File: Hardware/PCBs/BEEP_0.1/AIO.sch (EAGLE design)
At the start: 86 parts, among them IC1 ULN2803ASOP18, IC2 ULN2803ASOP18, IC3 74HC238SSOP, IC4 74HC238SSOP, U2 TB6612FNG, U3 ATXMEGA64D3-AU, X10 MICROMATCH-10, X3 MICROMATCH-8, X4 MICROMATCH-8, X5 MICROMATCH-8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

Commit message: continue routing...
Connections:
- net IR_LED_MK0: now also U3.PF0; no longer U3.PF2
- net IR_LED_MK2: now also U3.PF2; no longer U3.PF0
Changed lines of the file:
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@@
 </segment>
 <segment>
-<wire x1="93.98" y1="86.36" x2="88.9" y2="86.36" width="0.1524" layer="91" style="longdash"/>
-<label x="88.9" y="86.36" size="1.27" layer="95" rot="R180" xref="yes"/>
-<pinref part="U3" gate="G$1" pin="PF2"/>
+<wire x1="93.98" y1="91.44" x2="88.9" y2="91.44" width="0.1524" layer="91" style="longdash"/>
+<label x="88.9" y="91.44" size="1.27" layer="95" rot="R180" xref="yes"/>
+<pinref part="U3" gate="G$1" pin="PF0"/>
 </segment>
 </net>
@@
 </segment>
 <segment>
-<wire x1="93.98" y1="91.44" x2="88.9" y2="91.44" width="0.1524" layer="91" style="longdash"/>
-<label x="88.9" y="91.44" size="1.27" layer="95" rot="R180" xref="yes"/>
-<pinref part="U3" gate="G$1" pin="PF0"/>
+<wire x1="93.98" y1="86.36" x2="88.9" y2="86.36" width="0.1524" layer="91" style="longdash"/>
+<label x="88.9" y="86.36" size="1.27" layer="95" rot="R180" xref="yes"/>
+<pinref part="U3" gate="G$1" pin="PF2"/>
 </segment>
 </net>

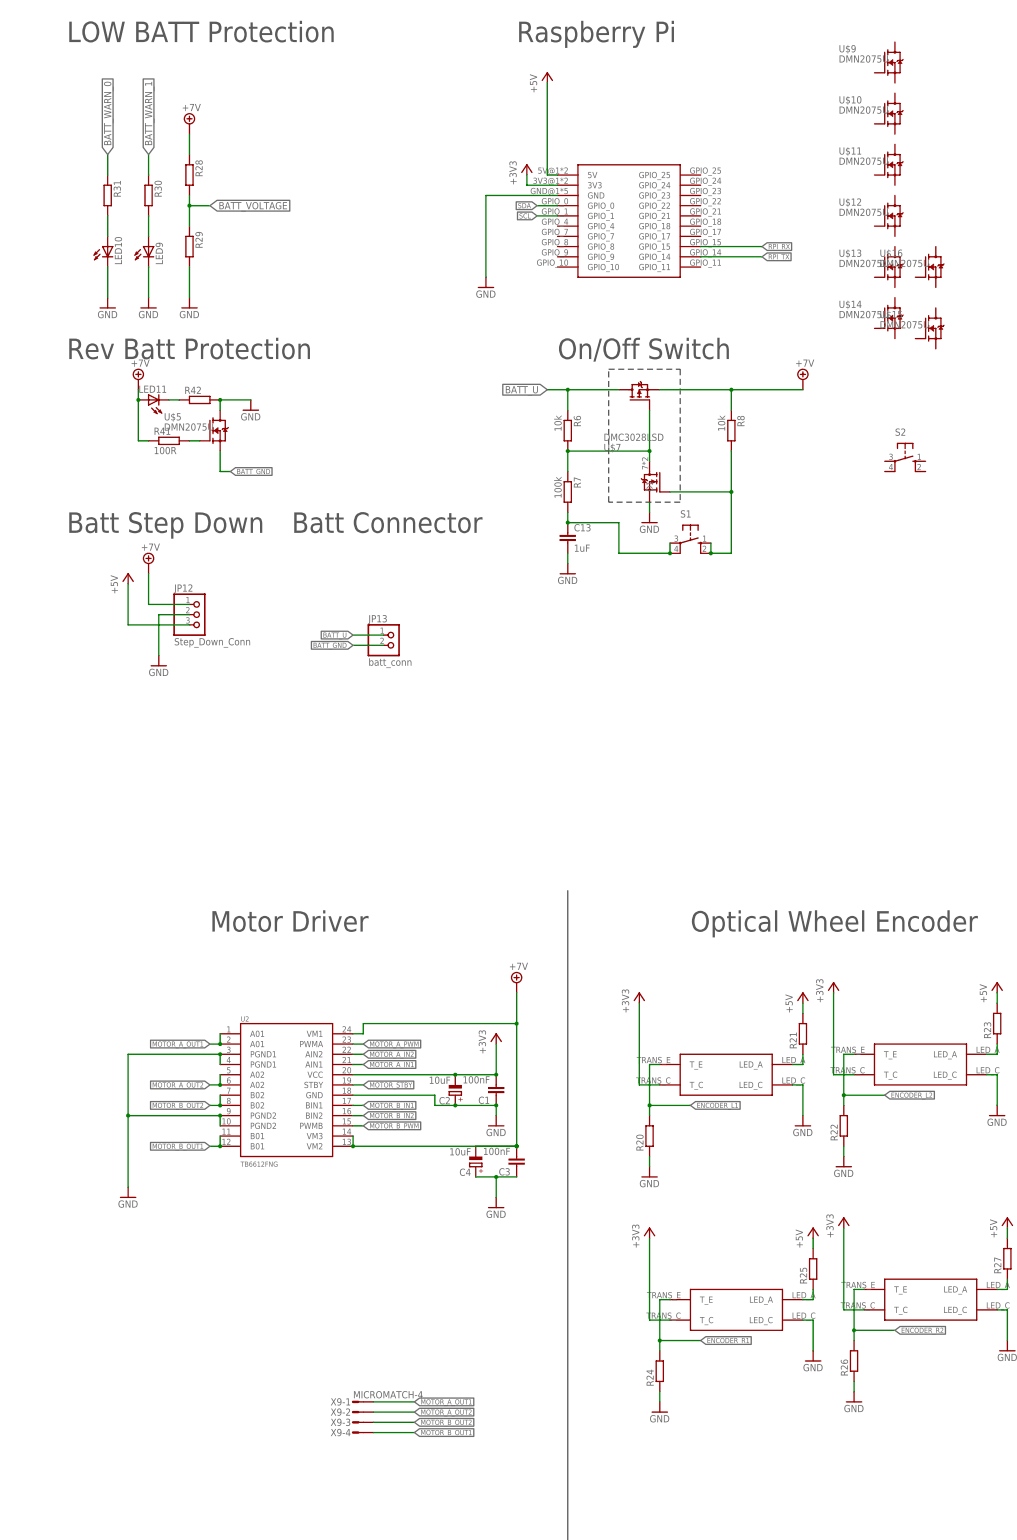
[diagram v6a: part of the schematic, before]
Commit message: Add audio amplifier correct batt rev circuit and on off circuit some routing
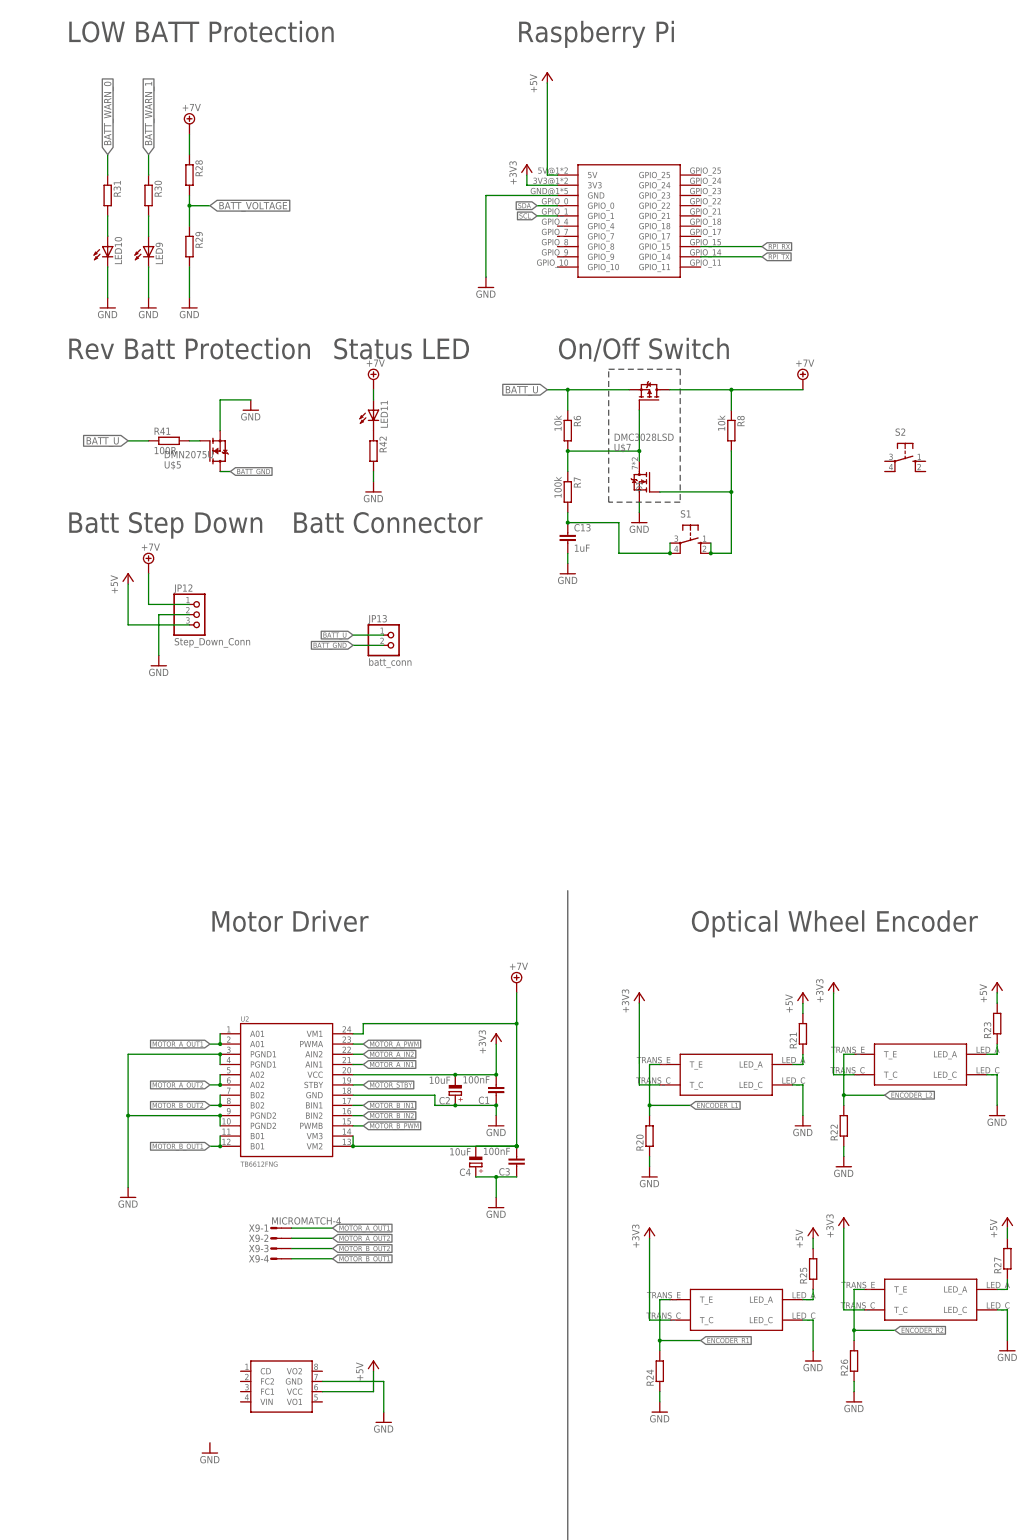
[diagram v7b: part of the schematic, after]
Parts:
- removed U$10, U$11, U$12, U$13, U$14, U$15, U$16, U$9: DMN2075U, BEEP:DMN2075U
- added IC5: TS34119SMD, BEEP:TS34119SMD
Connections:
- net +5V: now also IC5.VCC
- net +7V: now also U$7.D2; no longer R41.1, U$7.S2
- net BATT_GND: no longer U$5.S
- net BATT_U: now also R41.1, U$7.S2; no longer U$7.D2
- net GND: now also IC5.GND, U$5.S; no longer U$5.D
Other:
- note added: "Status LED"
- moved on the sheet: LED11, R42, U$5, U$7, X9-1, X9-2, X9-3, X9-4

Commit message: routing
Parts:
- added C14: 100nF, rcl:C-EUC0603
- added C15: 1uF, rcl:C-EUC0603
- added R10: 3k, rcl:R-EU_R0603
- added R9: 75k, rcl:R-EU_R0603
- added X1: MICROMATCH-4, Con-amp-micromatch:MICROMATCH-4
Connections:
- new net AUDIO_DISABLE: IC5.CD
- new net AUDIO_IN: C14.2, X1-3.S
- new net N$15: IC5.VIN, R10.1, R9.2
- new net N$17: C14.1, R10.2
- new net N$36: C15.1, IC5.FC2
- new net SPEAKER_O1: IC5.VO2, X1-1.S
- new net SPEAKER_O2: IC5.VO1, R9.1, X1-2.S
- net GND: now also C15.2, X1-4.S
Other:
- note added: "Audio amp"
- moved on the sheet: C1, C2, C3, C4, U2, X9-1, X9-2, X9-3, X9-4
